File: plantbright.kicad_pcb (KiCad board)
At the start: 2 copper layers, 33 x 54 mm, 23 parts, among them J1 POWER OUT, J2 USB-C, Q1 AO3400A, Q2 AO3400A, Q3 AO3400A, Q5 AO3400A, SW1 USER 0, U1 XIAO-ESP32-C6

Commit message: Add cap
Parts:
- added C1: 100uF, Capacitor_THT:CP_Radial_D5.0mm_P2.50mm, F.Cu at (152.1, 105.0)
- moved R9 13.7 mm to (155.4, 90.1), turned to 90 degrees
- moved Q1 1.09 mm to (166.4, 97.2)
- moved Q2 1.09 mm to (160.7, 97.4)
- moved R1 1.09 mm to (167.4, 92.9)
- moved R10 1.09 mm to (166.4, 102.9)
- moved R11 1.09 mm to (160.7, 102.9)
- moved R12 1.09 mm to (145.9, 102.8)
- moved R13 1.09 mm to (140.4, 102.8)
- moved R2 1.09 mm to (165.4, 92.9)
- moved R3 1.09 mm to (161.7, 92.9)
- moved R4 1.09 mm to (159.7, 92.9)
- moved Q3 1.09 mm to (145.9, 97.4)
- moved Q5 1.09 mm to (140.4, 97.5)
- moved R5 1.09 mm to (146.9, 92.9)
- moved R6 1.09 mm to (144.8, 92.9)
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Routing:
- net Net-(J1-Pin_5): track 19.4 -> 0.00 mm
- net Net-(J1-Pin_4): track 16.9 -> 0.03 mm
- net Net-(J1-Pin_3): track 5.13 -> 0.00 mm
- net Net-(J1-Pin_2): track 4.14 -> 0.00 mm
- net +5V: track 58.6 -> 62.5 mm
- net GND: track 31.7 -> 30.2 mm

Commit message: Ground pour
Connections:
- R10 pad 2: Net-(J1-Pin_2) -> Net-(J1-Pin_5)
- R11 pad 2: Net-(J1-Pin_3) -> Net-(J1-Pin_4)
- R12 pad 2: Net-(J1-Pin_4) -> Net-(J1-Pin_3)
- R13 pad 2: Net-(J1-Pin_5) -> Net-(J1-Pin_2)
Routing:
- net Net-(J1-Pin_2): track 0.00 -> 28.3 mm
- net Net-(J1-Pin_3): track 0.00 -> 23.1 mm
- net Net-(J1-Pin_4): track 0.03 -> 9.21 mm
- net Net-(J1-Pin_5): track 0.00 -> 8.78 mm
- added copper zone on B.Cu, net GND
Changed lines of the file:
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@@
 			(layers "F.Cu" "F.Mask" "F.Paste")
 			(roundrect_rratio 0.192308)
-			(net 26 "Net-(J1-Pin_4)")
+			(net 25 "Net-(J1-Pin_3)")
 			(pintype "passive")
 		)
@@
 			(layers "F.Cu" "F.Mask" "F.Paste")
 			(roundrect_rratio 0.192308)
-			(net 24 "Net-(J1-Pin_2)")
+			(net 23 "Net-(J1-Pin_5)")
 			(pintype "passive")
 		)
@@
 			(layers "F.Cu" "F.Mask" "F.Paste")
 			(roundrect_rratio 0.192308)
-			(net 25 "Net-(J1-Pin_3)")
+			(net 26 "Net-(J1-Pin_4)")
 			(pintype "passive")
 		)
@@
 			(layers "F.Cu" "F.Mask" "F.Paste")
 			(roundrect_rratio 0.192308)
-			(net 23 "Net-(J1-Pin_5)")
+			(net 24 "Net-(J1-Pin_2)")
 			(pintype "passive")
 		)
@@
 	)
 	(segment
+		(start 166.41 107.99)
+		(end 166.41 104.43744)
+		(width 0.5)
+		(layer "F.Cu")
+		(net 23)
+	)
+	(segment
+		(start 166.41 112.11)
+		(end 166.02 112.5)
+		(width 0.5)
+		(layer "F.Cu")
+		(net 23)
+	)
+	(segment
+		(start 166.02 108.38)
+		(end 166.41 107.99)
+		(width 0.5)
+		(layer "F.Cu")
+		(net 23)
+	)
+	(segment
+		(start 166.02 112.5)
+		(end 166.02 108.38)
+		(width 0.5)
+		(layer "F.Cu")
+		(net 23)
+	)
+	(segment
+		(start 149.801 103.3)
+		(end 155.3 103.3)
+		(width 0.5)
+		(layer "F.Cu")
+		(net 24)
+	)
+	(segment
+		(start 140.44 104.38744)
+		(end 140.44 105.54)
+		(width 0.5)
+		(layer "F.Cu")
+		(net 24)
+	)
+	(segment
+		(start 155.3 103.3)
+		(end 158.4 106.4)
+		(width 0.5)
+		(layer "F.Cu")
+		(net 24)
+	)
+	(segment
+		(start 140.44 105.54)
+		(end 141.5 106.6)
+		(width 0.5)
+		(layer "F.Cu")
+		(net 24)
+	)
+	(segment
+		(start 141.5 106.6)
+		(end 146.501 106.6)
+		(width 0.5)
+		(layer "F.Cu")
+		(net 24)
+	)
+	(segment
+		(start 146.501 106.6)
+		(end 149.801 103.3)
+		(width 0.5)
+		(layer "F.Cu")
+		(net 24)
+	)
+	(segment
+		(start 158.4 106.4)
+		(end 158.4 112.5)
+		(width 0.5)
+		(layer "F.Cu")
+		(net 24)
+	)
+	(segment
 		(start 145.94 104.38744)
 		(end 145.96256 104.41)
 		(width 0.5)
 		(layer "F.Cu")
+		(net 25)
+	)
+	(segment
+		(start 147.41256 104.38744)
+		(end 149.4 102.4)
+		(width 0.5)
+		(layer "F.Cu")
+		(net 25)
+	)
+	(segment
+		(start 149.4 102.4)
+		(end 156 102.4)
+		(width 0.5)
+		(layer "F.Cu")
+		(net 25)
+	)
+	(segment
+		(start 145.94 104.38744)
+		(end 147.41256 104.38744)
+		(width 0.5)
+		(layer "F.Cu")
+		(net 25)
+	)
+	(segment
+		(start 160.94 107.34)
+		(end 160.94 112.5)
+		(width 0.5)
+		(layer "F.Cu")
+		(net 25)
+	)
+	(segment
+		(start 156 102.4)
+		(end 160.94 107.34)
+		(width 0.5)
+		(layer "F.Cu")
+		(net 25)
+	)
+	(segment
+		(start 163.48 112.5)
+		(end 163.48 108.58)
+		(width 0.5)
+		(layer "F.Cu")
 		(net 26)
 	)
+	(segment
+		(start 163.48 108.58)
+		(end 160.71 105.81)
+		(width 0.5)
+		(layer "F.Cu")
+		(net 26)
+	)
+	(segment
+		(start 160.71 105.81)
+		(end 160.71 104.43744)
+		(width 0.5)
+		(layer "F.Cu")
+		(net 26)
+	)
+	(zone
+		(net 4)
+		(net_name "GND")
+		(layer "B.Cu")
+		(hatch edge 0.5)
+		(connect_pads
+			(clearance 0.5)
+		)
+		(min_thickness 0.25)
+		(filled_areas_thickness no)
+		(fill yes
+			(thermal_gap 0.5)
+			(thermal_bridge_width 0.5)
+		)
+		(polygon
+			(pts
+				(xy 166 79.5) (xy 169 88.5) (xy 169 117.5) (xy 137.5 117.5) (xy 137.541 88.464326) (xy 141 79.5)
+			)
+		)
+	)
 	(embedded_fonts no)

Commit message: DRC
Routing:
- net +5V: track 62.5 -> 57.3 mm
- net GND: track 30.2 -> 29.5 mm
- net Net-(J1-Pin_5): track 8.78 -> 8.22 mm
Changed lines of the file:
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@@
-	)
-	(segment
-		(start 155.13 112.5)
-		(end 155.86 112.5)
-		(width 0.5)
-		(layer "F.Cu")
-		(net 3)
 	)
 	(segment
@@
 	)
 	(segment
-		(start 147 108)
-		(end 142.5 108)
-		(width 0.5)
-		(layer "F.Cu")
-		(net 3)
-	)
-	(segment
 		(start 152.1 105.9)
 		(end 150 108)
@@
 		(start 144.99 96.45744)
 		(end 144.99 94.04494)
-		(width 0.2)
-		(layer "F.Cu")
-		(net 4)
-	)
-	(segment
-		(start 159.76 94.03744)
-		(end 159.6675 93.94494)
-		(width 0.2)
-		(layer "F.Cu")
-		(net 4)
-	)
-	(segment
-		(start 139.49 94.14494)
-		(end 139.24 93.89494)
-		(width 0.2)
-		(layer "F.Cu")
-		(net 4)
-	)
-	(segment
-		(start 144.99 94.04494)
-		(end 144.84 93.89494)
 		(width 0.2)
 		(layer "F.Cu")
@@
 	)
 	(segment
-		(start 166.41 112.11)
-		(end 166.02 112.5)
-		(width 0.5)
-		(layer "F.Cu")
-		(net 23)
-	)
-	(segment
 		(start 166.02 108.38)
 		(end 166.41 107.99)
@@
 	)
 	(segment
-		(start 145.94 104.38744)
-		(end 145.96256 104.41)
-		(width 0.5)
-		(layer "F.Cu")
-		(net 25)
-	)
-	(segment

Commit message: DRC, getting there.
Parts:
- C1: footprint Capacitor_THT:CP_Radial_D5.0mm_P2.50mm -> Capacitor_SMD:C_1206_3216Metric_Pad1.33x1.80mm_HandSolder
- R14, R15: moved to B.Cu
- moved R14 15.5 mm to (141.0, 102.7), turned to 90 degrees
- moved C1 8.61 mm to (151.8, 113.6), turned to -90 degrees
- moved R15 7.91 mm to (141.0, 106.8), turned to 90 degrees
- moved SW1 2.80 mm to (155.3, 96.8)
- moved R9 2.80 mm to (155.4, 92.9)
- moved J2 1.12 mm to (143.7, 114.2)
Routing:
- net Net-(J2-CC2): track 7.27 -> 18.7 mm, vias 0 -> 1
- net CH_1: track 2.03 -> 11.0 mm
- net CH_4: track 2.20 -> 10.5 mm
- net BTN_1: track 9.45 -> 16.6 mm
- net CH_2: track 2.04 -> 7.92 mm
- net CH_3: track 2.10 -> 7.80 mm
- net Net-(J1-Pin_2): track 28.3 -> 22.9 mm
- net Net-(J2-CC1): track 7.77 -> 11.8 mm, vias 0 -> 1
- net +3.3V: track 24.6 -> 28.5 mm
- net Net-(J1-Pin_3): track 23.0 -> 19.9 mm
- net GND: track 29.5 -> 28.4 mm
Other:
- board text removed: "I AM A CONSTANT VOLTAGE DEVICE. PLEASE DON'T USE HIGH-POWER LEDs."

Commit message: Yay, V1.
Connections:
- U1 pad 10: unconnected-(U1-GPIO20/D9/MISO-Pad10) -> CH_3
- U1 pad 11: unconnected-(U1-GPIO18/D10/MOSI-Pad11) -> CH_4
- U1 pad 3: CH_3 -> BTN_1
- U1 pad 4: CH_4 -> unconnected-(U1-GPIO21/D3-Pad4)_1
- U1 pad 5: BTN_1 -> unconnected-(U1-GPIO22/D4/SDA-Pad5)
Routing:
- net CH_3: track 7.80 -> 23.3 mm
- net BTN_1: track 16.6 -> 29.7 mm
- net CH_4: track 10.5 -> 22.8 mm
- net CH_2: track 7.92 -> 13.8 mm
- net CH_1: track 11.0 -> 13.1 mm
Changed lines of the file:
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@@
 	(net 28 "unconnected-(U1-GPIO17{slash}D7{slash}RX-Pad8)")
 	(net 29 "unconnected-(U1-GPIO17{slash}D7{slash}RX-Pad8)_1")
-	(net 30 "unconnected-(U1-GPIO20{slash}D9{slash}MISO-Pad10)")
+	(net 30 "unconnected-(U1-GPIO22{slash}D4{slash}SDA-Pad5)")
 	(net 31 "unconnected-(U1-GPIO19{slash}D8{slash}SCK-Pad9)_1")
-	(net 32 "unconnected-(U1-GPIO18{slash}D10{slash}MOSI-Pad11)")
+	(net 32 "unconnected-(U1-GPIO21{slash}D3-Pad4)")
 	(net 33 "unconnected-(U1-GPIO23{slash}D5{slash}SCL-Pad6)")
-	(net 34 "unconnected-(U1-GPIO18{slash}D10{slash}MOSI-Pad11)_1")
+	(net 34 "unconnected-(U1-GPIO21{slash}D3-Pad4)_1")
 	(net 35 "unconnected-(U1-GPIO16{slash}D6{slash}TX-Pad7)")
 	(net 36 "unconnected-(U1-GPIO16{slash}D6{slash}TX-Pad7)_1")
 	(net 37 "unconnected-(U1-GPIO23{slash}D5{slash}SCL-Pad6)_1")
-	(net 38 "unconnected-(U1-GPIO20{slash}D9{slash}MISO-Pad10)_1")
+	(net 38 "unconnected-(U1-GPIO22{slash}D4{slash}SDA-Pad5)_1")
 	(footprint "Resistor_SMD:R_1206_3216Metric_Pad1.30x1.75mm_HandSolder"
 		(layer "F.Cu")
@@
 			(layers "F.Cu" "F.Mask")
 			(roundrect_rratio 0.1)
-			(net 14 "CH_3")
+			(net 16 "BTN_1")
 			(pinfunction "GPIO2/A2/D2")
 			(pintype "passive")
@@
 			(layers "*.Cu" "*.Mask")
 			(remove_unused_layers no)
-			(net 14 "CH_3")
+			(net 16 "BTN_1")
 			(pinfunction "GPIO2/A2/D2")
 			(pintype "passive")
@@
 			(layers "F.Cu" "F.Mask")
 			(roundrect_rratio 0.1)
-			(net 15 "CH_4")
+			(net 32 "unconnected-(U1-GPIO21{slash}D3-Pad4)")
 			(pinfunction "GPIO21/D3")
-			(pintype "passive")
+			(pintype "passive+no_connect")
 			(thermal_bridge_angle 45)
 		)
@@
 			(layers "*.Cu" "*.Mask")
 			(remove_unused_layers no)
-			(net 15 "CH_4")
+			(net 34 "unconnected-(U1-GPIO21{slash}D3-Pad4)_1")
 			(pinfunction "GPIO21/D3")
-			(pintype "passive")
+			(pintype "passive+no_connect")
 		)
 		(pad "5" smd roundrect
@@
 			(layers "F.Cu" "F.Mask")
 			(roundrect_rratio 0.1)
-			(net 16 "BTN_1")
+			(net 38 "unconnected-(U1-GPIO22{slash}D4{slash}SDA-Pad5)_1")
 			(pinfunction "GPIO22/D4/SDA")
-			(pintype "passive")
+			(pintype "passive+no_connect")
 			(thermal_bridge_angle 45)
 		)
@@
 			(layers "*.Cu" "*.Mask")
 			(remove_unused_layers no)
-			(net 16 "BTN_1")
+			(net 30 "unconnected-(U1-GPIO22{slash}D4{slash}SDA-Pad5)")
 			(pinfunction "GPIO22/D4/SDA")
-			(pintype "passive")
+			(pintype "passive+no_connect")
 		)
 		(pad "6" smd roundrect
@@
 			(layers "*.Cu" "*.Mask")
 			(remove_unused_layers no)
-			(net 38 "unconnected-(U1-GPIO20{slash}D9{slash}MISO-Pad10)_1")
+			(net 14 "CH_3")
 			(pinfunction "GPIO20/D9/MISO")
-			(pintype "passive+no_connect")
+			(pintype "passive")
 		)
 		(pad "10" smd roundrect
@@
 			(layers "F.Cu" "F.Mask")
 			(roundrect_rratio 0.1)
-			(net 30 "unconnected-(U1-GPIO20{slash}D9{slash}MISO-Pad10)")
+			(net 14 "CH_3")
 			(pinfunction "GPIO20/D9/MISO")
-			(pintype "passive+no_connect")
+			(pintype "passive")
 			(thermal_bridge_angle 45)
 		)
@@
 			(layers "*.Cu" "*.Mask")
 			(remove_unused_layers no)
-			(net 34 "unconnected-(U1-GPIO18{slash}D10{slash}MOSI-Pad11)_1")
+			(net 15 "CH_4")
 			(pinfunction "GPIO18/D10/MOSI")
-			(pintype "passive+no_connect")
+			(pintype "passive")
 		)
 		(pad "11" smd roundrect
@@
 			(layers "F.Cu" "F.Mask")
 			(roundrect_rratio 0.1)
-			(net 32 "unconnected-(U1-GPIO18{slash}D10{slash}MOSI-Pad11)")
+			(net 15 "CH_4")
 			(pinfunction "GPIO18/D10/MOSI")
-			(pintype "passive+no_connect")
+			(pintype "passive")
 			(thermal_bridge_angle 45)
 		)
@@
 	)
 	(segment
+		(start 154.3 90.8)
+		(end 155.4 91.9)
+		(width 0.2)
+		(layer "F.Cu")
+		(net 4)
+	)
+	(segment
 		(start 139.49 98.42)
 		(end 139.49 96.45744)
@@
 	)
 	(segment
+		(start 153.1 90.8)
+		(end 154.3 90.8)
+		(width 0.2)
+		(layer "F.Cu")
+		(net 4)
+	)
+	(segment
 		(start 144.0275 95.49494)
 		(end 143.24 95.49494)
@@
 	)
 	(segment
-		(start 156.5 91.9)
-		(end 155.4 91.9)
-		(width 0.2)
-		(layer "F.Cu")
-		(net 4)
-	)
-	(segment
 		(start 140.43 110.105)
 		(end 140.275 110.105)
@@
 		(net 4)
 	)
-	(segment
-		(start 157.6 93)
-		(end 156.5 91.9)
-		(width 0.2)
-		(layer "F.Cu")
-		(net 4)
-	)
 	(via
 		(at 143.24 95.49494)
@@
 	)
 	(via
-		(at 157.6 93)
+		(at 153.1 90.8)
 		(size 0.6)
 		(drill 0.3)
@@
 	)
 	(segment
-		(start 165.3575 91.2575)
-		(end 159.5 85.4)
+		(start 161.14 87.72744)
+		(end 165.3575 91.94494)
 		(width 0.2)
 		(layer "F.Cu")
@@
 	)
 	(segment
+		(start 161.14 83.34)
+		(end 161.14 87.72744)
+		(width 0.2)
+		(layer "F.Cu")
+		(net 12)
+	)
+	(segment
 		(start 159.6675 91.94494)
 		(end 159.6675 88.5675)
@@
 	)
 	(segment
-		(start 159.6675 88.5675)
-		(end 157.9 86.8)
+		(start 159.6675 82.2725)
+		(end 161.14 80.8)
 		(width 0.2)
 		(layer "F.Cu")
@@
 	)
 	(segment
-		(start 144.84 91.89494)
-		(end 146.94 91.89494)
+		(start 159.6675 88.5675)
+		(end 159.6675 82.2725)
 		(width 0.2)
 		(layer "F.Cu")
-		(net 14)
+		(net 13)
 	)
 	(segment
-		(start 146.94 88.26)
-		(end 148.4 86.8)
+		(start 146.94 85.76)
+		(end 148.4 84.3)
 		(width 0.2)
 		(layer "F.Cu")
@@
 	(segment
 		(start 146.94 91.89494)
-		(end 146.94 88.26)
+		(end 146.94 85.76)
+		(width 0.2)
+		(layer "F.Cu")
+		(net 14)
+	)
+	(segment
+		(start 148.4 84.3)
+		(end 148.4 74.3)
+		(width 0.2)
+		(layer "F.Cu")
+		(net 14)
+	)
+	(segment
+		(start 148.4 74.3)
+		(end 147.28 73.18)
+		(width 0.2)
+		(layer "F.Cu")
+		(net 14)
+	)
+	(segment
+		(start 147.28 73.18)
+		(end 145.9 73.18)
+		(width 0.2)
+		(layer "F.Cu")
+		(net 14)
+	)
+	(segment
+		(start 144.84 91.89494)
+		(end 146.94 91.89494)
 		(width 0.2)
 		(layer "F.Cu")
@@
 	)
 	(segment
+		(start 148 84.1)
+		(end 148 76.5)
+		(width 0.2)
+		(layer "F.Cu")
+		(net 15)
+	)
+	(segment
+		(start 141.39 90.71)
+		(end 148 84.1)
+		(width 0.2)
+		(layer "F.Cu")
+		(net 15)
+	)
+	(segment
 		(start 141.39 91.89494)
 		(end 141.39 90.71)
@@
 	)
 	(segment
-		(start 141.39 90.71)
-		(end 146.4 85.7)
+		(start 148 76.5)
+		(end 147.22 75.72)
 		(width 0.2)
 		(layer "F.Cu")
@@
 	)
 	(segment
+		(start 147.22 75.72)
+		(end 145.9 75.72)
+		(width 0.2)
+		(layer "F.Cu")
+		(net 15)
+	)
+	(segment
+		(start 159.2 90.1)
+		(end 159.2 79)
+		(width 0.2)
+		(layer "F.Cu")
+		(net 16)
+	)
+	(segment
 		(start 155.4 93.9)
-		(end 153.2 91.7)
+		(end 159.2 90.1)
 		(width 0.2)
 		(layer "F.Cu")
@@
 	)
 	(segment
+		(start 159.2 79)
+		(end 159.94 78.26)
+		(width 0.2)
+		(layer "F.Cu")
+		(net 16)
+	)
+	(segment
 		(start 155.35 96.85)
 		(end 155.35 98.4)
@@
 	)
 	(segment
-		(start 153.2 91.7)
-		(end 153.2 89.2)
+		(start 159.94 78.26)
+		(end 161.14 78.26)
 		(width 0.2)
 		(layer "F.Cu")

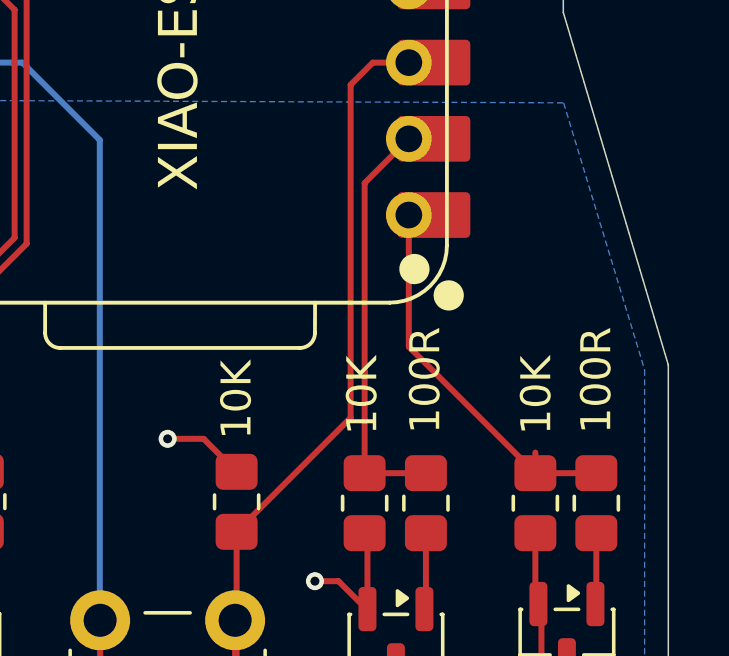
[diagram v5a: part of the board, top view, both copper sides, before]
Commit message: Merge colinear tracks
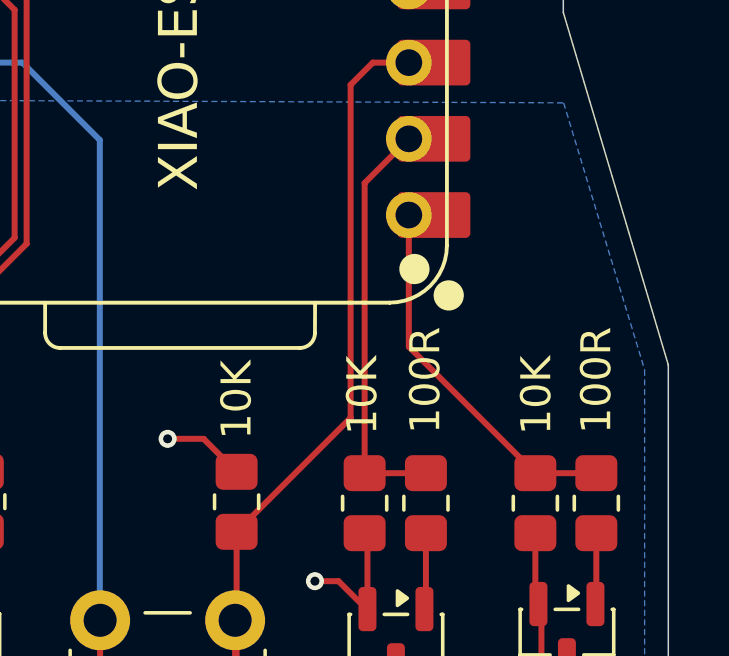
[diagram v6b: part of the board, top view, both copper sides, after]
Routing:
- net CH_1: track 13.1 -> 12.4 mm
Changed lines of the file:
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@@
-	)
-	(segment
-		(start 165.3575 91.94494)
-		(end 165.3575 91.2575)
-		(width 0.2)
-		(layer "F.Cu")
-		(net 12)
 	)
 	(segment
@@
 		(layer "F.Cu")
 		(net 12)
-	)
-	(segment
-		(start 159.6675 91.94494)
-		(end 159.6675 88.5675)
-		(width 0.2)
-		(layer "F.Cu")
-		(net 13)
 	)
 	(segment
@@
 	)
 	(segment
-		(start 159.6675 88.5675)
+		(start 159.6675 91.94494)
 		(end 159.6675 82.2725)
 		(width 0.2)

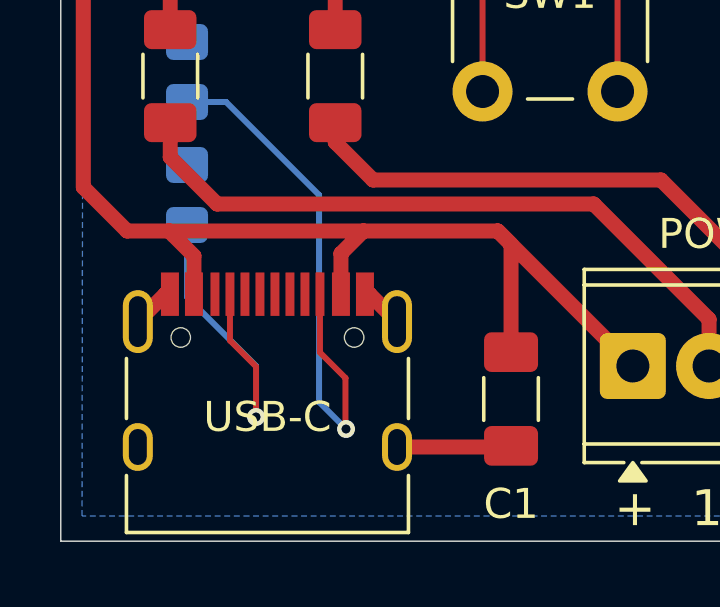
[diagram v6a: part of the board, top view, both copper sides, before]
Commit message: Move vias away from silkscreen
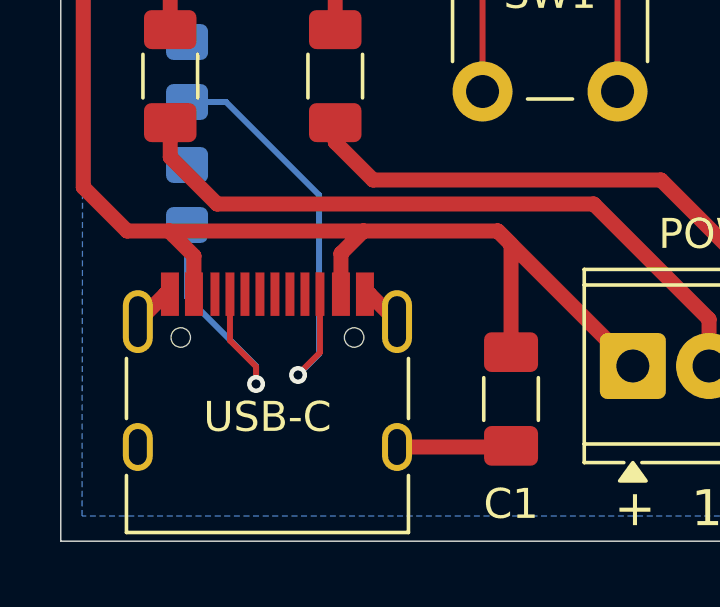
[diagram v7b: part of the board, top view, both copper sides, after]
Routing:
- net Net-(J2-CC2): track 18.7 -> 15.0 mm
- net Net-(J2-CC1): track 11.8 -> 9.61 mm
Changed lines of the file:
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@@
+	)
+	(segment
+		(start 142.43 111.65)
+		(end 142.43 110.105)
+		(width 0.2)
+		(layer "F.Cu")
+		(net 20)
 	)
 	(segment
@@
 	)
 	(segment
-		(start 143.3 114.2)
+		(start 143.3 113.1)
 		(end 143.3 112.52)
 		(width 0.2)
@@
 		(net 20)
 	)
-	(segment
-		(start 142.43 111.65)
-		(end 142.43 110.105)
-		(width 0.2)
-		(layer "F.Cu")
-		(net 20)
-	)
 	(via
-		(at 143.3 114.2)
+		(at 143.3 113.1)
 		(size 0.6)
 		(drill 0.3)
@@
 	)
 	(segment
-		(start 141 110.2)
+		(start 143.3 113.1)
 		(end 143.3 112.5)
 		(width 0.2)
@@
 	)
 	(segment
-		(start 141 107.8)
+		(start 141 110.2)
+		(end 141 107.8)
+		(width 0.2)
+		(layer "B.Cu")
+		(net 20)
+	)
+	(segment
+		(start 143.3 112.5)
 		(end 141 110.2)
 		(width 0.2)
@@
 	)
 	(segment
-		(start 143.3 112.5)
-		(end 143.3 114.2)
+		(start 144.7 112.78)
+		(end 145.43 112.05)
 		(width 0.2)
-		(layer "B.Cu")
-		(net 20)
+		(layer "F.Cu")
+		(net 21)
+	)
+	(segment
+		(start 144.7 112.8)
+		(end 144.7 112.78)
+		(width 0.2)
+		(layer "F.Cu")
+		(net 21)
 	)
 	(segment
@@
 		(net 21)
 	)
-	(segment
-		(start 146.28 112.9)
-		(end 145.43 112.05)
-		(width 0.2)
-		(layer "F.Cu")
+	(via
+		(at 144.7 112.8)
+		(size 0.6)
+		(drill 0.3)
+		(layers "F.Cu" "B.Cu")
 		(net 21)
 	)
 	(segment
-		(start 146.3 114.6)
-		(end 146.28 114.58)
+		(start 142.3 103.7)
+		(end 141 103.7)
 		(width 0.2)
-		(layer "F.Cu")
-		(net 21)
-	)
-	(segment
-		(start 146.28 114.58)
-		(end 146.28 112.9)
-		(width 0.2)
-		(layer "F.Cu")
-		(net 21)
-	)
-	(via
-		(at 146.3 114.6)
-		(size 0.6)
-		(drill 0.3)
-		(layers "F.Cu" "B.Cu")
+		(layer "B.Cu")
 		(net 21)
 	)
@@
 	)
 	(segment
-		(start 146.3 114.6)
-		(end 145.4 113.7)
+		(start 145.4 112.1)
+		(end 145.4 106.8)
 		(width 0.2)
 		(layer "B.Cu")
@@
 	)
 	(segment
-		(start 142.3 103.7)
-		(end 141 103.7)
+		(start 144.7 112.8)
+		(end 145.4 112.1)
 		(width 0.2)
 		(layer "B.Cu")
-		(net 21)
-	)
-	(segment
-		(start 145.4 113.7)
-		(end 145.4 106.8)
-		(width 0.2)
-		(layer "B.Cu")

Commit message: Update plantbright.kicad_pcb
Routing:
- net Net-(J2-CC1): track 9.61 -> 8.45 mm
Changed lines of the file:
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@@
-		(net 20)
-	)
-	(segment
-		(start 143.3 113.1)
-		(end 143.3 112.52)
-		(width 0.2)
-		(layer "F.Cu")
 		(net 20)
 	)
 	(via
-		(at 143.3 113.1)
+		(at 143.3 112.52)
 		(size 0.6)
 		(drill 0.3)
@@
 	)
 	(segment
-		(start 143.3 113.1)
-		(end 143.3 112.5)
+		(start 143.3 112.5)
+		(end 141 110.2)
 		(width 0.2)
 		(layer "B.Cu")
@@
 	)
 	(segment
-		(start 143.3 112.5)
-		(end 141 110.2)
+		(start 143.3 112.52)
+		(end 143.3 112.5)
 		(width 0.2)
 		(layer "B.Cu")
